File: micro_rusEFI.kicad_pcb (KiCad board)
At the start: 2 copper layers, 80.6 x 93.7 mm, 256 parts, among them J1 USB_B_Micro, J12 Conn_01x01, J13 Conn_01x01, J15 Conn_01x01, J17 Conn_01x01, J19 Conn_01x06, J2 Conn_02x05_Odd_Even, J3 Conn_01x01, J4 Conn_02x05_Counter_Clockwise, J5 Conn_01x01, J7 TC2030, Q1 IPD30N06S2L-23, SW1 SW_Push, SW2 SW_Push, SW3 SW_Push, SW4 SW_Push, U1 STM32F427VGT6, U10 VNLD5090, U11 IS25LP256D-xM, U2 TLE8888QK, U3 molex_48pin_MRE, U31 MIC4427, U32 MIC4427, U33 MIC4427, U35 MCP6004, U36 MCP6004, U4 TLE9201SG, U46 MCP6004, U5 LM1117-3.3, U6 W25Q128JVSIQ, U7 XC6206 3.3V, U8 MCP6004, U9 VNLD5090, X1 8MHz 20pF, Y2 32768 Hz

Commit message: First commit
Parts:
- removed C1, C13, C14, C15, C17, C18, C42, C6, C78: 100nF, Capacitor_SMD:C_0603_1608Metric
- removed C12, C35: 1nF, Capacitor_SMD:C_0603_1608Metric
- removed C19: 10nF, Capacitor_SMD:C_0603_1608Metric
- removed C3: 4.7nF, Capacitor_SMD:C_0603_1608Metric
- removed C4, C5: 470nF, Capacitor_SMD:C_0603_1608Metric
- removed C41: 2.2uF, Capacitor_SMD:C_0603_1608Metric
- removed C43: 22uF 25V, Capacitor_SMD:C_0805_2012Metric
- removed C7: 10uF, Capacitor_SMD:C_0603_1608Metric
- removed D1: BAV70, Package_TO_SOT_SMD:SOT-23
- removed D15, D20, D3, D4, D5, D6: SS54, Diode_SMD:D_SMA
- removed D2: PESD1CAN-UX, Package_TO_SOT_SMD:SOT-23
- removed D28, D31, D33, D35: LED-RED, LED_SMD:LED_0603_1608Metric
- removed D30, D32, D34, D43: 1N4148WS, Diode_SMD:D_SOD-323
- removed G***: LOGO, rusefi_lib:mre_logo
- removed J12, J13, J15, J17, J3, J5: Conn_01x01, Connector_Pin:Pin_D0.7mm_L6.5mm_W1.8mm_FlatFork
- removed JP2: High side voltage 5V 12V, Jumper:SolderJumper-3_P1.3mm_Open_Pad1.0x1.5mm
- removed R1, R12, R13, R16, R4, R6: 10K, Resistor_SMD:R_0603_1608Metric
- removed R10: 1k, Resistor_SMD:R_1206_3216Metric
- removed R120, R121, R122, R123, R124, R125: 100, Resistor_SMD:R_1206_3216Metric
- removed R15: 15k, Resistor_SMD:R_0603_1608Metric
- removed R17, R18, R19: DNP, Resistor_SMD:R_0603_1608Metric
- removed R2: 0R DNP, Resistor_SMD:R_0603_1608Metric
- removed R20: 2.7k, Resistor_SMD:R_0603_1608Metric
- removed R22: 120, Resistor_SMD:R_0805_2012Metric
- removed R29, R36, R49, R51: 1k, Resistor_SMD:R_0603_1608Metric
- removed R3: 10K, Resistor_SMD:R_0805_2012Metric
- removed R30, R8, R84, R85: 0R, Resistor_SMD:R_0603_1608Metric
- removed R42, R82, R83, R9: 4.7K, Resistor_SMD:R_0603_1608Metric
- removed R86: 0R, Resistor_SMD:R_0805_2012Metric
- removed RN5, RN6: 10k, Resistor_SMD:R_Array_Convex_4x0603
- removed TP4: TP, TestPoint:TestPoint_Pad_D2.0mm
- removed U10, U9: VNLD5090, Package_SO:SO-8_3.9x4.9mm_P1.27mm
- removed U11: IS25LP256D-xM, Package_SO:SOIC-16W_7.5x10.3mm_P1.27mm
- removed U2: TLE8888QK, Package_QFP:LQFP-100_14x14mm_P0.5mm_THERMAL
- removed U31, U32, U33: MIC4427, Package_SO:SOIC-8_3.9x4.9mm_P1.27mm
- removed U4: TLE9201SG, Package_SO:Infineon_PG-DSO-12-11
- removed U6: W25Q128JVSIQ, hw_microRusEfi-master:SO-8_5.3x6.2mm_P1.27mm-150+208
- removed U7: XC6206 3.3V, Package_TO_SOT_SMD:SOT-23
- moved FID3 22.4 mm to (88.9, 38.1)
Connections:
- net /MCU/USB_VBUS renamed /MCU/PA9
- net /SCK renamed /MCU/PB3
- net /TLE8888-1QK/IGN_OUT_1 renamed Net-(R21-Pad2)
- net /TLE8888-1QK/IGN_OUT_2 renamed Net-(R33-Pad2)
- net /TLE8888-1QK/IGN_OUT_3 renamed Net-(R80-Pad2)
- net /TLE8888-1QK/IGN_OUT_4 renamed Net-(R81-Pad2)
- U1 pad 38: /TLE8888-1QK/IN_12 -> /MCU/PE7
- U1 pad 39: /TLE8888-1QK/IN_11 -> /MCU/PE8
- U1 pad 40: /TLE8888-1QK/IN_10 -> /MCU/PE9
- U1 pad 41: /TLE8888-1QK/IN_9 -> /MCU/PE10
- U1 pad 42: /TLE8888-1QK/INJ_IN_4 -> /MCU/PE11
- U1 pad 43: /TLE8888-1QK/INJ_IN_3 -> /MCU/PE12
- U1 pad 44: /TLE8888-1QK/INJ_IN_2 -> /MCU/PE13
- U1 pad 45: /TLE8888-1QK/INJ_IN_1 -> /MCU/PE14
- U1 pad 46: /FlashMemory/CS -> /MCU/PE15
- U1 pad 51: /TLE8888-1QK/CAN_RX -> /MCU/PB12
- U1 pad 55: /TLE8888-1QK/LIN_TX -> /MCU/PD8
- U1 pad 56: /TLE8888-1QK/LIN_RX -> /MCU/PD9
- U1 pad 57: /TLE8888-1QK/IGN_EN -> /MCU/PD10
- U1 pad 58: /TLE8888-1QK/INJ_EN -> /MCU/PD11
- U1 pad 59: /PD12 -> /MCU/PD12
- U1 pad 60: /PD13 -> /MCU/PD13
- U1 pad 61: /PD14 -> /MCU/PD14
- U1 pad 62: /PD15 -> /MCU/PD15
- U1 pad 63: /CRANK -> /MCU/PC6
- U1 pad 65: /H-BRIDGE/DIS -> /MCU/PC8
- U1 pad 67: /H-BRIDGE/DIR -> /MCU/PA8
- U1 pad 82: /hi-lo/Ign4_MCU -> /MCU/PD1
- U1 pad 83: /hi-lo/Ign3_MCU -> /MCU/PD2
- U1 pad 84: /hi-lo/Ign2_MCU -> /MCU/PD3
- U1 pad 85: /hi-lo/Ign1_MCU -> /MCU/PD4
- U1 pad 86: /CS_TLE -> /MCU/PD5
- U1 pad 87: /hi-lo/GP6_MCU -> /MCU/PD6
- U1 pad 88: /hi-lo/GP5_MCU -> /MCU/PD7
- U1 pad 90: /SO -> /MCU/PB4
- U1 pad 91: /SI -> /MCU/PB5
- U1 pad 92: /TLE8888-1QK/CAN_TX -> /MCU/PB6
- U3 pad 10: /Ign2 -> unconnected-(U3-Pad10)
- U3 pad 11: /Ign3 -> unconnected-(U3-Pad11)
- U3 pad 12: /Ign4 -> unconnected-(U3-Pad12)
- U3 pad 13: /GP6 -> unconnected-(U3-Pad13)
- U3 pad 14: /GP5 -> unconnected-(U3-Pad14)
- U3 pad 3: /LS2 -> unconnected-(U3-Pad3)
- U3 pad 33: /GP3 -> unconnected-(U3-Pad33)
- U3 pad 34: /GP2 -> unconnected-(U3-Pad34)
- U3 pad 35: /GP1 -> unconnected-(U3-Pad35)
- U3 pad 37: /INJECTOR-1 -> unconnected-(U3-Pad37)
- U3 pad 38: /INJECTOR-2 -> unconnected-(U3-Pad38)
- U3 pad 4: /E-THROTTLE+ -> unconnected-(U3-Pad4)
- U3 pad 41: /INJECTOR-3 -> unconnected-(U3-Pad41)
- U3 pad 42: /INJECTOR-4 -> unconnected-(U3-Pad42)
- U3 pad 43: /GP4 -> unconnected-(U3-Pad43)
- U3 pad 45: /CRNK+ -> unconnected-(U3-Pad45)
- U3 pad 46: /CRNK- -> unconnected-(U3-Pad46)
- U3 pad 7: /LS1 -> unconnected-(U3-Pad7)
- U3 pad 8: /E-THROTTLE- -> unconnected-(U3-Pad8)
- U3 pad 9: /Ign1 -> unconnected-(U3-Pad9)
- U3 pad J14: /TLE8888-1QK/OUT_7 -> unconnected-(U3-PadJ14)
- U3 pad J61: /TLE8888-1QK/OUT_14 -> (no net)
- U3 pad J62: /TLE8888-1QK/OUT_15 -> (no net)
- U3 pad J63: /TLE8888-1QK/OUT_16 -> (no net)
- U3 pad J64: /TLE8888-1QK/OUT_17 -> (no net)
- U3 pad J65: /TLE8888-1QK/OUT_18 -> (no net)
- U3 pad LIN1: /LINBUS -> (no net)
- U3 pad M11: (no net) -> unconnected-(U3-PadM11)
- U3 pad M12: (no net) -> unconnected-(U3-PadM12)
- U3 pad M13: (no net) -> unconnected-(U3-PadM13)
- U3 pad M21: (no net) -> unconnected-(U3-PadM21)
- U3 pad M22: (no net) -> unconnected-(U3-PadM22)
- U3 pad M23: (no net) -> unconnected-(U3-PadM23)
- U3 pad M3: (no net) -> unconnected-(U3-PadM3)
- U3 pad M4: (no net) -> unconnected-(U3-PadM4)
- U3 pad M51: (no net) -> unconnected-(U3-PadM51)
- U3 pad M52: (no net) -> unconnected-(U3-PadM52)
- U3 pad M53: (no net) -> unconnected-(U3-PadM53)
- U3 pad M61: (no net) -> unconnected-(U3-PadM61)
- U3 pad M62: (no net) -> unconnected-(U3-PadM62)
- U3 pad M63: (no net) -> unconnected-(U3-PadM63)
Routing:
- net (no net): track 0.00 -> 434.4 mm, vias 0 -> 15
- net unconnected-(U3-Pad3): track 0.00 -> 106.9 mm, vias 0 -> 4
- net /LS2: track 106.9 -> 0.00 mm, vias 4 -> 0
- net unconnected-(U3-Pad7): track 0.00 -> 94.2 mm, vias 0 -> 3
- net /LS1: track 94.2 -> 0.00 mm, vias 3 -> 0
- net unconnected-(U3-Pad35): track 0.00 -> 83.1 mm, vias 0 -> 2
- net /GP1: track 83.1 -> 0.00 mm, vias 2 -> 0
- net unconnected-(U3-Pad34): track 0.00 -> 80.5 mm, vias 0 -> 2
- net /GP2: track 80.5 -> 0.00 mm, vias 2 -> 0
- net unconnected-(U3-Pad37): track 0.00 -> 72.8 mm
- net /INJECTOR-1: track 72.8 -> 0.00 mm
- net unconnected-(U3-Pad33): track 0.00 -> 72.6 mm, vias 0 -> 2
- net /GP3: track 72.6 -> 0.00 mm, vias 2 -> 0
- net unconnected-(U3-Pad38): track 0.00 -> 71.4 mm, vias 0 -> 1
- net /INJECTOR-2: track 71.4 -> 0.00 mm, vias 1 -> 0
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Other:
- outline, holes or cut-outs redrawn
- net class 1A EXTERNAL removed
- net class 2.5A EXTERNAL removed
- net class 3,5A EXT HIGH VOLTAGE removed
- net class 3.5A EXTERNAL removed
- net class 5A EXTERNAL removed
- net class CUSTOM removed
- net class CUSTOM 0.6 removed
- net class Default removed
- net class MIN_EXTERN_188A removed
- net class MIN_EXTERN_241A removed
- board text removed: "4"
- board text removed: "5"
- board text removed: "Hall"
- board text removed: "INJ1"
- board text removed: "LS2"
- board text removed: "TC4427"
- board text removed: "TLE8888"
- board text removed: "on when hi/lo GP5 is driving low"

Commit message: First commit
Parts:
- removed J4: Conn_02x05_Counter_Clockwise, Connector_PinHeader_2.54mm:PinHeader_2x05_P2.54mm_Vertical_SMD
- removed R21, R33, R80, R81: 0R, Resistor_SMD:R_0603_1608Metric
- added C1: 4.7u, Capacitor_SMD:C_0603_1608Metric, F.Cu at (91.4, 71.1)
- added C3: 1u, Capacitor_SMD:C_0603_1608Metric, F.Cu at (87.4, 71.1)
- added C4: 10n, Capacitor_SMD:C_0603_1608Metric, F.Cu at (87.4, 73.6)
- added C6: 270p, Capacitor_SMD:C_0603_1608Metric, F.Cu at (83.4, 71.1)
- added C7: 10u, Capacitor_SMD:C_0603_1608Metric, F.Cu at (83.4, 73.6)
- added C8: 10u, Capacitor_SMD:C_0603_1608Metric, F.Cu at (83.4, 76.1)
- added R2: 10k, Resistor_SMD:R_0402_1005Metric, F.Cu at (89.8, 75.9)
- added R3: 12k, Resistor_SMD:R_0402_1005Metric, F.Cu at (86.9, 75.9)
- added R4: 68k, Resistor_SMD:R_0402_1005Metric, F.Cu at (90.9, 73.4)
- moved TP12 75.9 mm to (99.3, 84.2)
- moved FID5 20.7 mm to (88.9, 38.1)
- moved TP0 12.0 mm to (29.0, 85.3)
- moved R131 10.9 mm to (50.5, 41.0)
- moved R56 10.3 mm to (67.3, 41.0)
- moved R37 10.2 mm to (61.6, 43.6), turned to -90 degrees
- moved TP3 9.30 mm to (29.1, 88.3)
- moved R31 9.11 mm to (63.5, 40.0)
- moved C16 8.46 mm to (68.3, 51.2), turned to -90 degrees
- moved C2 8.38 mm to (85.4, 85.1), turned to 90 degrees
- moved R24 7.70 mm to (64.9, 41.1)
- moved TP5 6.62 mm to (29.0, 82.1)
- moved R41 5.47 mm to (55.2, 40.4)
- moved C45 5.14 mm to (68.3, 49.1), turned to -90 degrees
- moved C46 4.72 mm to (68.6, 47.3)
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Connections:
- C2 pad 1: /12V_SAFE -> Net-(2.2u1-Pad2)
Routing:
- net (no net): track 434.4 -> 0.00 mm, vias 15 -> 0
- net /5V: track 467.3 -> 320.7 mm, vias 25 -> 14
- net unconnected-(U3-Pad3): track 106.9 -> 0.00 mm, vias 4 -> 0
- net /VDD: track 298.4 -> 193.7 mm, vias 33 -> 29
- net /12V_MREL: track 229.9 -> 131.6 mm, vias 16 -> 7
- net unconnected-(U3-Pad7): track 94.2 -> 0.00 mm, vias 3 -> 0
- net /MAIN_RELAY: track 92.0 -> 0.00 mm
- net /12V_SAFE: track 140.7 -> 49.0 mm, vias 57 -> 51
- net unconnected-(U3-Pad35): track 83.1 -> 0.00 mm, vias 2 -> 0
- net Net-(R33-Pad2): track 81.9 -> 0.00 mm, vias 3 -> 0
- net unconnected-(U3-Pad34): track 80.5 -> 0.00 mm, vias 2 -> 0
- net Net-(R21-Pad2): track 78.8 -> 0.00 mm, vias 3 -> 0
- net Net-(R80-Pad2): track 75.7 -> 0.00 mm, vias 2 -> 0
- net Net-(R81-Pad2): track 74.9 -> 0.00 mm, vias 2 -> 0
- net unconnected-(U3-Pad37): track 72.8 -> 0.10 mm
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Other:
- outline, holes or cut-outs redrawn

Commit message: did stuff
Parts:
- removed C10: 100nF, Capacitor_SMD:C_0603_1608Metric
- removed C11: 4.7nF, Capacitor_SMD:C_0603_1608Metric
- removed the C8 at (84.3, 94.0)
- removed C9: 10uF, Capacitor_SMD:C_0603_1608Metric
- removed Q1: IPD30N06S2L-23, Package_TO_SOT_SMD:TO-252-2
- added 10u1: L_Small, Inductor_SMD:L_1210_3225Metric, F.Cu at (82.6, 65.2)
- added 2.2u1: INDUCTOR, Simon:MWSA0503, F.Cu at (76.2, 63.5)
- added C5: 100n, Capacitor_SMD:C_0603_1608Metric, F.Cu at (89.2, 56.7)
- added D1: D_Schottky, Diode_SMD:D_SMA, F.Cu at (76.7, 57.8)
- added R1: 1, Resistor_SMD:R_0402_1005Metric, F.Cu at (88.6, 59.0)
- added U2: LMR14020, Simon:SOIC8-DFN, F.Cu at (79.0, 109.9)
- U3: footprint rusefi_lib:Molex_48_MRE -> rusefi_lib:Molex_48_BCM
- moved D41 15.6 mm to (86.2, 86.0), turned to 90 degrees
- moved C2 12.4 mm to (91.7, 95.8), turned to 0 degrees
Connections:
- C2 pad 1: Net-(2.2u1-Pad2) -> /12V_SAFE
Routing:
- net /12V_SAFE: track 49.0 -> 14.2 mm, vias 51 -> 10
- net /TLE8888-1QK/V6V: track 7.01 -> 0.00 mm
- net /TLE8888-1QK/V6GATE: track 3.89 -> 0.00 mm
- net GND: vias 314 -> 228

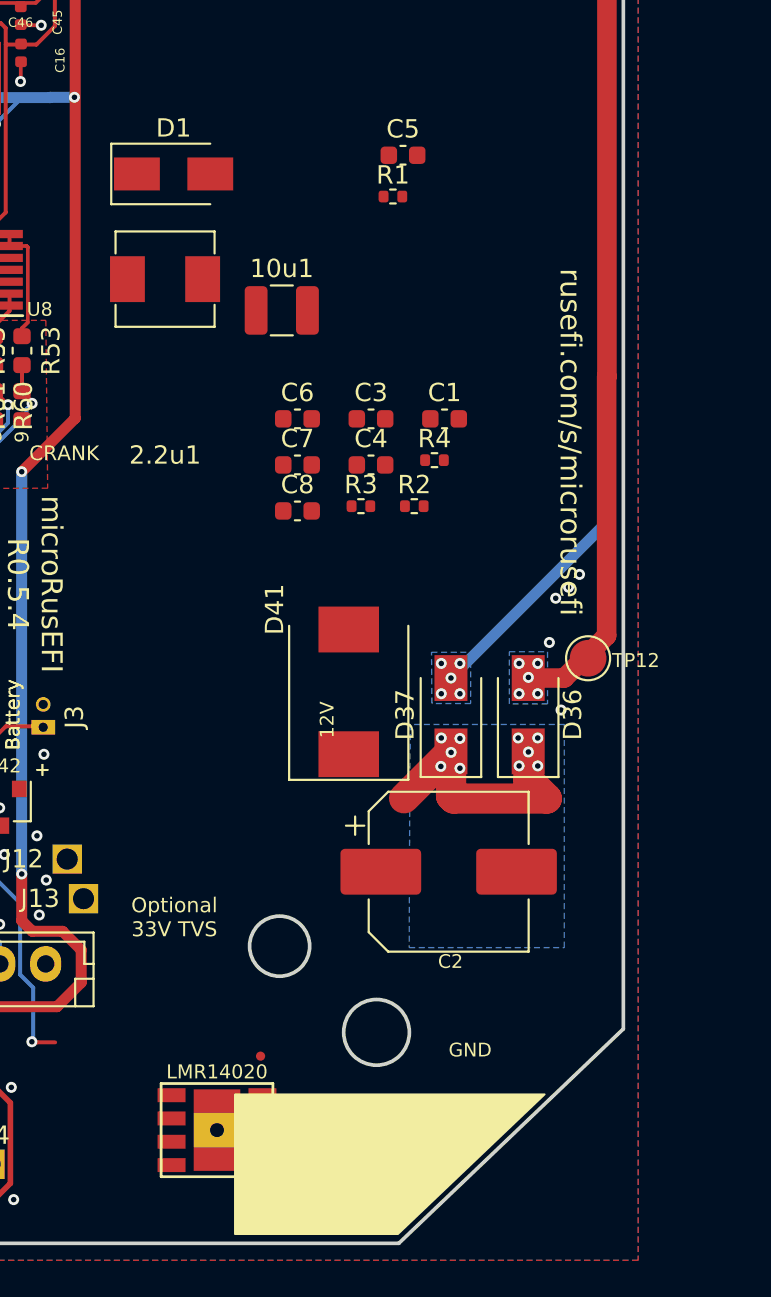
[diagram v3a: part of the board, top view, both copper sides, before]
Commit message: arranging 5v
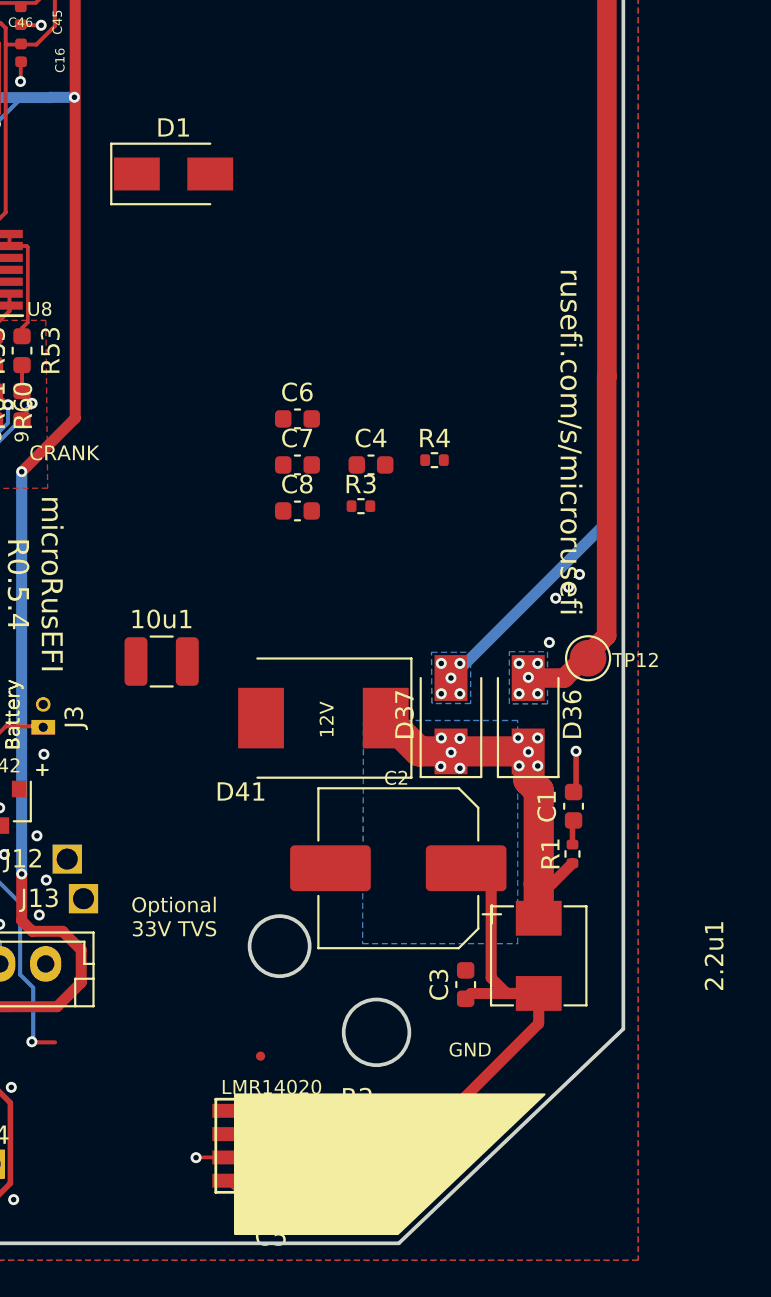
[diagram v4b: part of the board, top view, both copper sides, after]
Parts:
- moved C5 58.0 mm to (82.0, 114.3), turned to 180 degrees
- moved 2.2u1 42.2 mm to (96.6, 100.4), turned to 90 degrees
- moved R1 37.2 mm to (98.4, 94.8), turned to 90 degrees
- moved R2 33.6 mm to (86.7, 109.3)
- moved C3 31.3 mm to (92.6, 102.0), turned to 90 degrees
- moved C1 22.3 mm to (98.5, 92.2), turned to 90 degrees
- moved 10u1 20.2 mm to (76.0, 84.3)
- moved U2 3.10 mm to (82.0, 110.8)
- moved C2 2.75 mm to (88.9, 95.6), turned to 180 degrees
- moved D41 1.99 mm to (84.8, 87.4), turned to 180 degrees
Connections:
- C2 pad 1: /12V_SAFE -> Net-(2.2u1-Pad2)
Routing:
- net Net-(2.2u1-Pad2): track 0.00 -> 38.2 mm
- net GND: track 87.5 -> 96.8 mm, vias 228 -> 231
- net /12V_SAFE: track 14.2 -> 20.1 mm
- net Net-(C5-Pad1): track 0.00 -> 2.41 mm
- net Net-(10u1-Pad1): track 0.00 -> 2.35 mm
- net Net-(R2-Pad1): track 0.00 -> 1.93 mm
- net Net-(C1-Pad1): track 0.00 -> 1.34 mm

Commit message: 5v stage improved
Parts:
- moved D1 54.3 mm to (70.3, 111.7), turned to -90 degrees
- moved C4 41.1 mm to (73.6, 112.4), turned to -90 degrees
- moved R4 36.9 mm to (76.3, 107.3)
- moved C7 36.1 mm to (72.9, 108.2), turned to -90 degrees
- moved C6 35.9 mm to (74.3, 105.8)
- moved C8 33.3 mm to (74.6, 108.2), turned to -90 degrees
- moved R3 32.6 mm to (78.3, 107.4)
- moved 10u1 22.3 mm to (70.3, 105.9), turned to 90 degrees
- moved R1 18.4 mm to (90.4, 111.5), turned to 45 degrees
- moved C1 18.3 mm to (92.4, 109.5), turned to 45 degrees
- moved 2.2u1 15.4 mm to (85.9, 111.5), turned to 0 degrees
- moved FID4 12.6 mm to (93.4, 102.1)
- moved C2 12.1 mm to (77.6, 99.9), turned to 90 degrees
- moved C3 11.4 mm to (82.0, 106.2)
- moved D41 10.7 mm to (90.2, 96.6)
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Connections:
- 10u1 pad 2: /TLE8888-1QK/5V -> /5V
- C6 pad 1: /TLE8888-1QK/5V -> /5V
- C7 pad 1: /TLE8888-1QK/5V -> /5V
- C8 pad 1: /TLE8888-1QK/5V -> /5V
- R4 pad 1: /TLE8888-1QK/5V -> /5V
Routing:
- net Net-(2.2u1-Pad2): track 38.2 -> 16.9 mm
- net GND: track 96.8 -> 116.4 mm, vias 231 -> 234
- net /5V: track 320.7 -> 335.4 mm
- net /12V_SAFE: track 20.1 -> 34.3 mm
- net Net-(10u1-Pad1): track 2.35 -> 15.3 mm
- net Net-(C6-Pad2): track 0.00 -> 6.84 mm
- net Net-(C4-Pad1): track 0.00 -> 3.61 mm
- removed copper zone on B.Cu, net /12V_SAFE
